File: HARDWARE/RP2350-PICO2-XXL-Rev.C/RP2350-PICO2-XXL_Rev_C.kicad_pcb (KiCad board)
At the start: 4 copper layers, 100 x 100 mm, 62 parts, among them Q1 Q12MHz/18pF/30ppm/4P/3.2x2.5m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, U1 W25Q128JVSIQ(SOIC-8_208mils), U3 RP2350B(QFN-80_10.00x10.00x0.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, U4 NA(W25Q128JVSIQ(SOIC-8_208mil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, U5 APS6404L-3SQR-SN(SOIC-8_150mi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

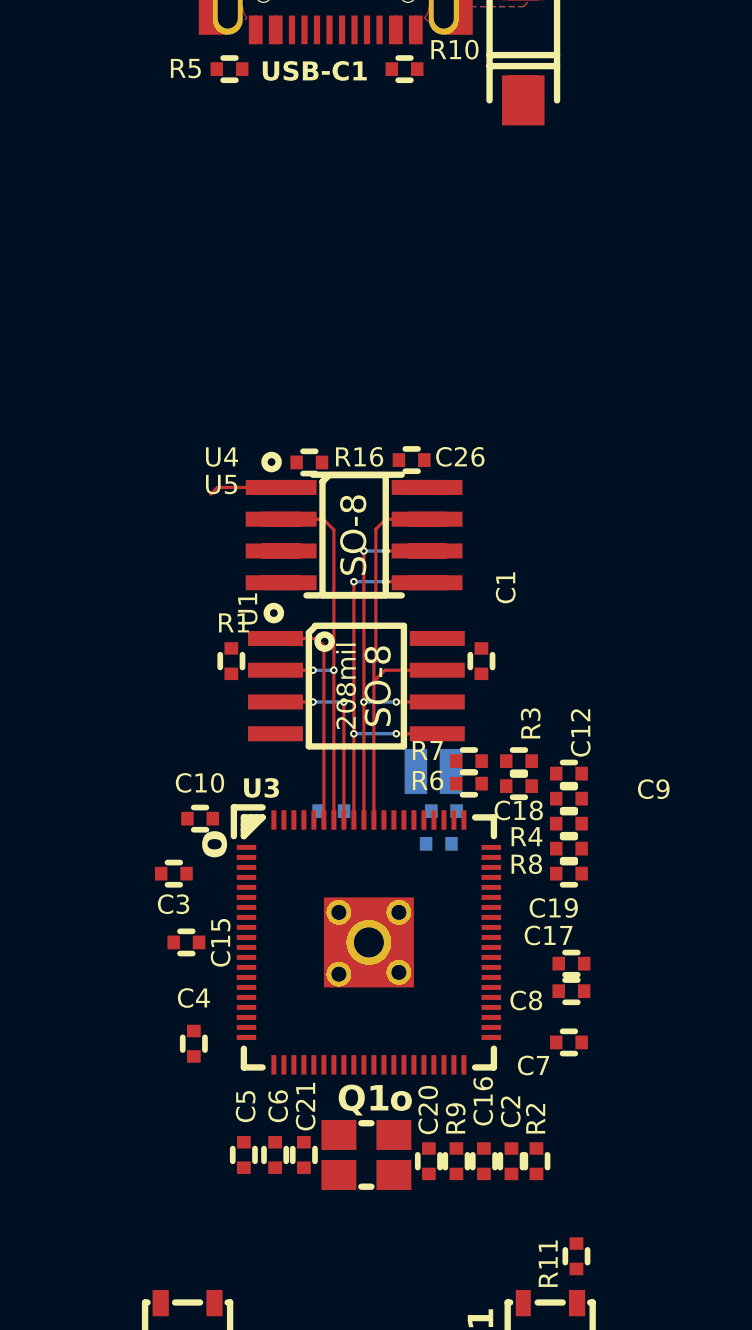
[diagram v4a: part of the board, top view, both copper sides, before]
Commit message: wip: routing bypass capacitors
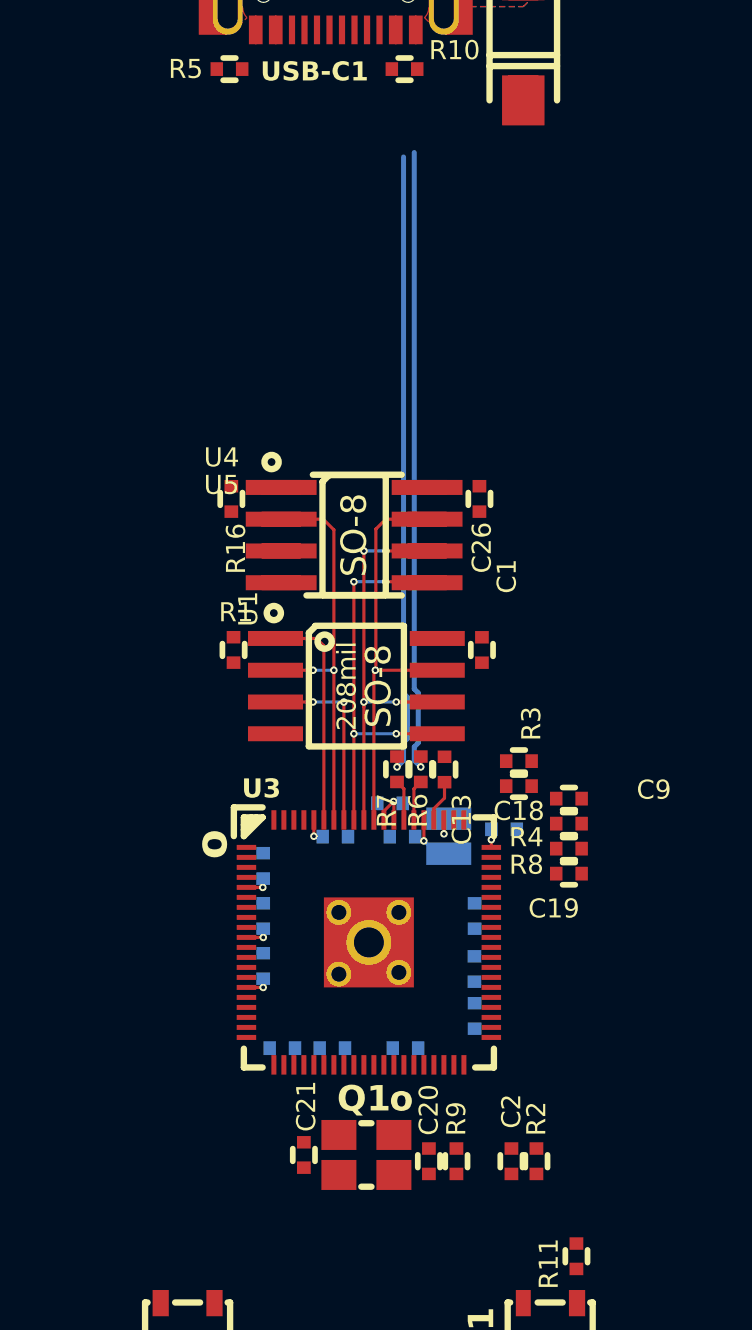
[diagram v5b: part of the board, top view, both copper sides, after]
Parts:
- C10, C12, C15, C16, C17, C3, C4, C5, C6, C7, C8: moved to B.Cu
- C13: moved to F.Cu
- moved C10 7.62 mm to (83.2, 55.9)
- moved C16 5.50 mm to (83.8, 65.7), turned to 0 degrees
- moved C6 4.85 mm to (80.9, 65.7), turned to 180 degrees
- moved C5 4.54 mm to (78.9, 65.7), turned to 180 degrees
- moved C17 4.32 mm to (86.6, 60.4), turned to 90 degrees
- moved C4 4.17 mm to (78.1, 62.4), turned to 90 degrees
- moved C8 3.98 mm to (86.5, 62.5), turned to -90 degrees
- moved C7 3.92 mm to (86.6, 64.4), turned to 90 degrees
- moved C3 3.58 mm to (78.1, 58.4), turned to 90 degrees
- moved R16 3.44 mm to (76.8, 43.7), turned to 90 degrees
- moved C12 3.42 mm to (87.7, 56.9)
- moved C15 3.25 mm to (78.1, 60.4), turned to 90 degrees
- moved C26 3.12 mm to (86.7, 43.7), turned to 90 degrees
- moved R7 2.89 mm to (83.4, 54.5), turned to -90 degrees
- moved L1 2.66 mm to (85.5, 57.2), turned to 90 degrees
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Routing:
- net /USB_D-: track 0.00 -> 25.2 mm, vias 0 -> 1
- net /USB_D+: track 0.00 -> 25.1 mm, vias 0 -> 1
- net +3.3V: track 0.00 -> 7.50 mm, vias 0 -> 5
- net /+1V1: track 0.00 -> 3.49 mm, vias 0 -> 2
- net /GPIO8\QMI_CS1n: track 3.25 -> 0.00 mm
- net /D+: track 0.00 -> 1.63 mm
- net /D-: track 0.00 -> 1.63 mm
- net Net-(U3-VREG_LX): track 0.00 -> 1.25 mm, vias 0 -> 1
- net /QSPI_SD3: track 16.3 -> 16.0 mm, vias 0 -> 1

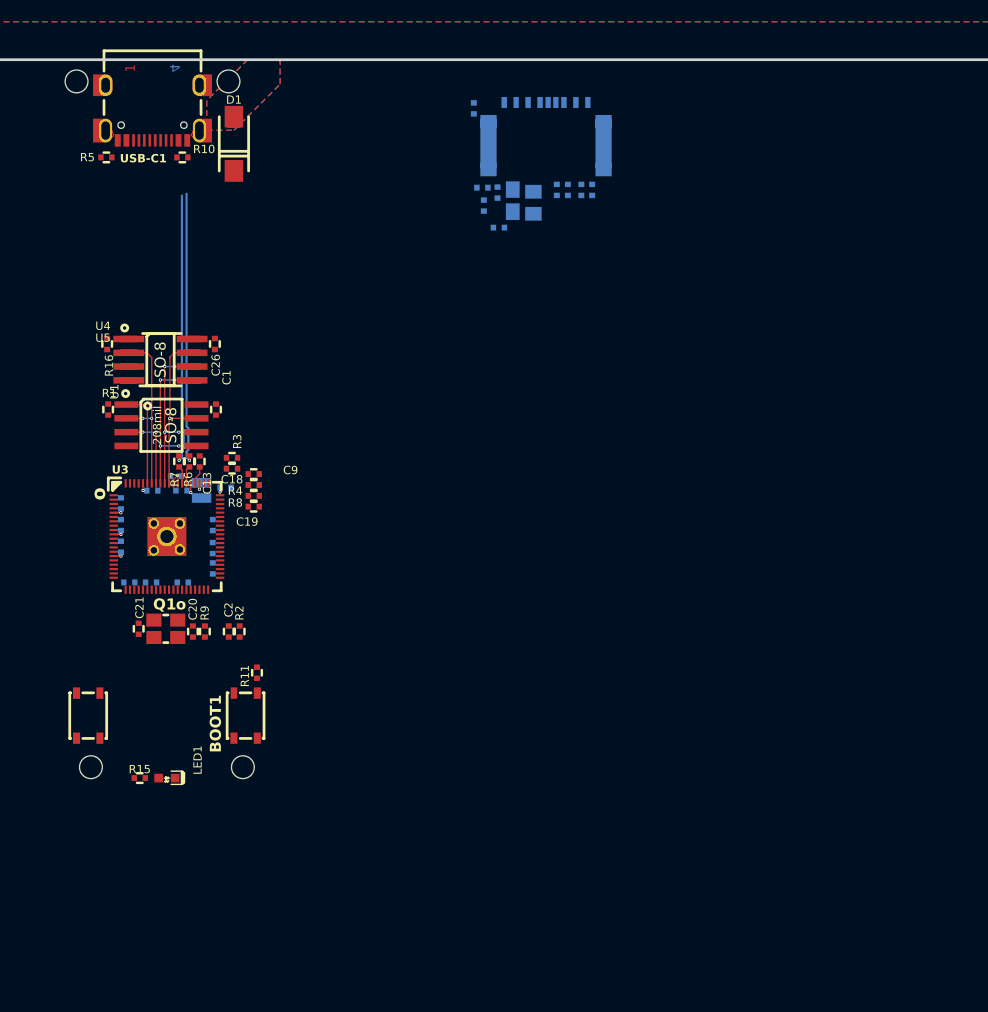
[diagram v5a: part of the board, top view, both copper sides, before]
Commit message: WIP: osc placed, need to add global osc with match length timing
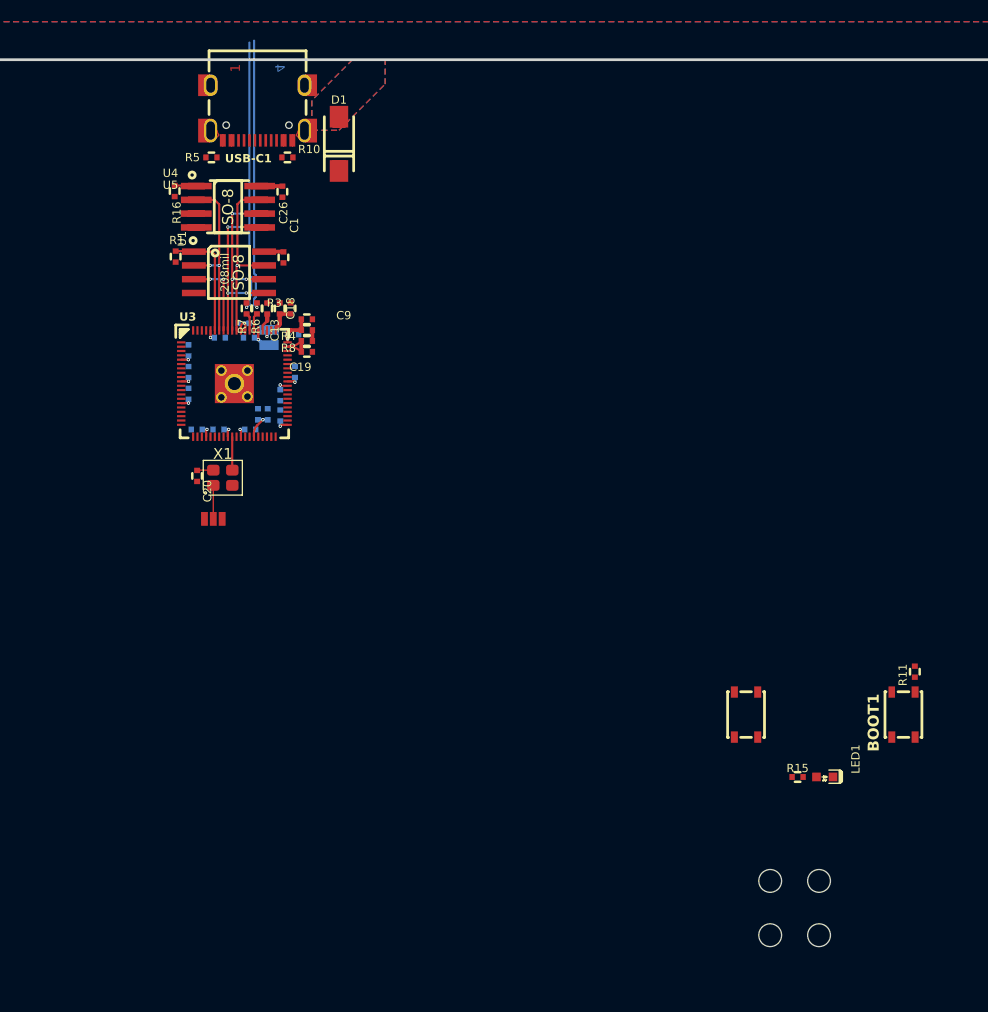
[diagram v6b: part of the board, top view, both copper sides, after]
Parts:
- removed C21: 27pF/50V/5%/C0G/C0402, OLIMEX_RLC-FP:C_0402_5MIL_DWS
- removed C27: 47uF/6.3V/20%/X5R/C0805, OLIMEX_RLC-FP:C_0805_5MIL_DWS
- removed L3: FB0805/600R/2A, OLIMEX_RLC-FP:L_0805_5MIL_DWS
- removed MICRO_SD1: TFC-9P-1.7H(ATFFS150A01BR016), OLIMEX_Connectors-FP:uSD(TFC-9P-1.xH(ATFFS150A01BR016))
- removed Q1: Q12MHz/18pF/30ppm/4P/3.2x2.5mm(ABM8-12.000MHZ-D2Y-T), OLIMEX_Crystal-FP:TSX-3.2x2.5mm_GND(3)
- removed R19, R20, R21, R22, R23: 10k/R0402, OLIMEX_RLC-FP:R_0402_5MIL_DWS
- removed R24, R25, R26: 33R/R0402, OLIMEX_RLC-FP:R_0402_5MIL_DWS
- removed R27: NA, OLIMEX_RLC-FP:R_0402_5MIL_DWS
- removed R9: 1k/R0402, OLIMEX_RLC-FP:R_0402_5MIL_DWS
- added JP1: ~, PCM_SparkFun-Jumper:Jumper_3_NO_NoSilk, F.Cu at (86.6, 59.8)
- added X1: SMD2520-4, PCM_Crystal_AKL:Crystal_SMD_2520-4Pin_2.5x2.0mm, F.Cu at (87.5, 56.0)
- C2, R2: moved to B.Cu
- C20: value 27pF/50V/5%/C0G/C0402 -> 100nF/10V/20%/X5R/C0402; footprint OLIMEX_RLC-FP:C_0402_5MIL_DWS -> KiCad:C_0402_5MIL_DWS
- moved MH3 97.5 mm to (137.9, 93.2)
- moved MH4 91.6 mm to (142.4, 93.2)
- moved MH1 64.5 mm to (137.9, 98.2)
- moved BOOT1 60.6 mm to (150.2, 77.8)
- moved LED1 60.6 mm to (142.9, 83.6)
- moved R15 60.6 mm to (140.4, 83.6)
- moved RST1 60.6 mm to (135.7, 77.8)
- moved R11 60.6 mm to (151.2, 73.9)
- moved MH2 55.3 mm to (142.4, 98.2)
- moved C2 20.2 mm to (90.7, 50.2), turned to 90 degrees
- moved R2 20.2 mm to (91.6, 50.2), turned to -90 degrees
- moved C17 16.0 mm to (94.1, 46.3)
- moved C18 15.4 mm to (92.7, 40.4), turned to 90 degrees
- moved C16 15.4 mm to (90.0, 51.6)
- moved C3 15.4 mm to (84.3, 44.3)
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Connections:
- C20 pad 1: Net-(C20-Pad1) -> GND
- C20 pad 2: GND -> +3.3V
- U3 pad 31: Net-(U3-XOUT) -> unconnected-(U3-XOUT-Pad31)
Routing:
- net +3.3V: track 7.50 -> 20.6 mm, vias 5 -> 9
- net /ADC_AVDD: track 0.00 -> 3.80 mm
- net Net-(U3-XIN): track 0.00 -> 3.08 mm
- net Net-(JP1-B): track 0.00 -> 2.85 mm
- net /RUN: track 0.00 -> 2.78 mm, vias 0 -> 1
- net /+1V1: track 3.49 -> 5.95 mm, vias 2 -> 4
- net /GPIO8\QMI_CS1n: track 0.00 -> 2.32 mm
- net /VREG_AVDD: track 0.00 -> 2.30 mm
- net /QSPI_CSn: track 9.02 -> 10.7 mm
- net /ADC_VREF: track 0.00 -> 1.00 mm
- added copper zone on F.Cu, net /VREG_AVDD
